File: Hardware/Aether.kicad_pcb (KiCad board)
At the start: 2 copper layers, 66.5 x 26 mm, 83 parts, among them J1 PRGM, J2 CONN-2, J3 CONN-2, J4 CONN-2, J5 CONN-2, J6 CONN-3, J7 CONN-3, Q1 IRLML6401, U1 ANTENOVA-UB, U2 ADF7012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

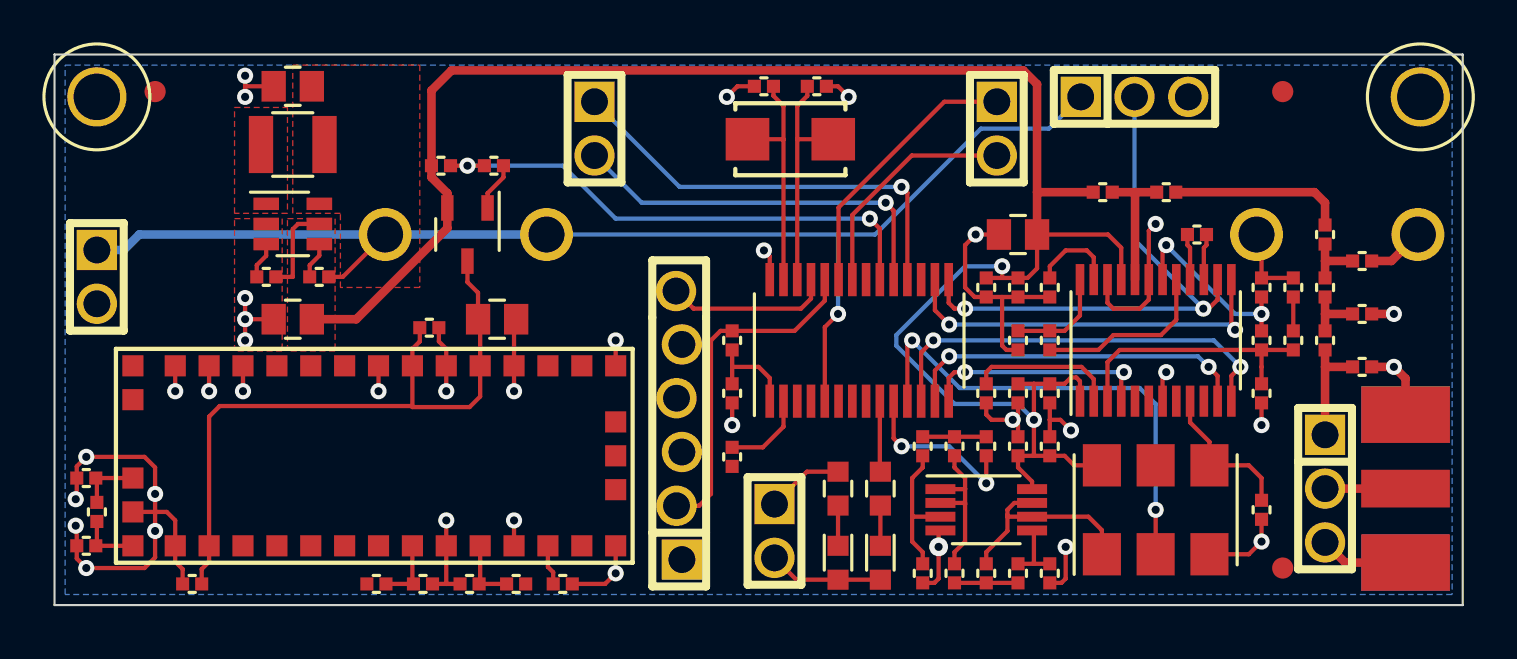
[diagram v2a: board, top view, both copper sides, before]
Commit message: Add RF ground pour
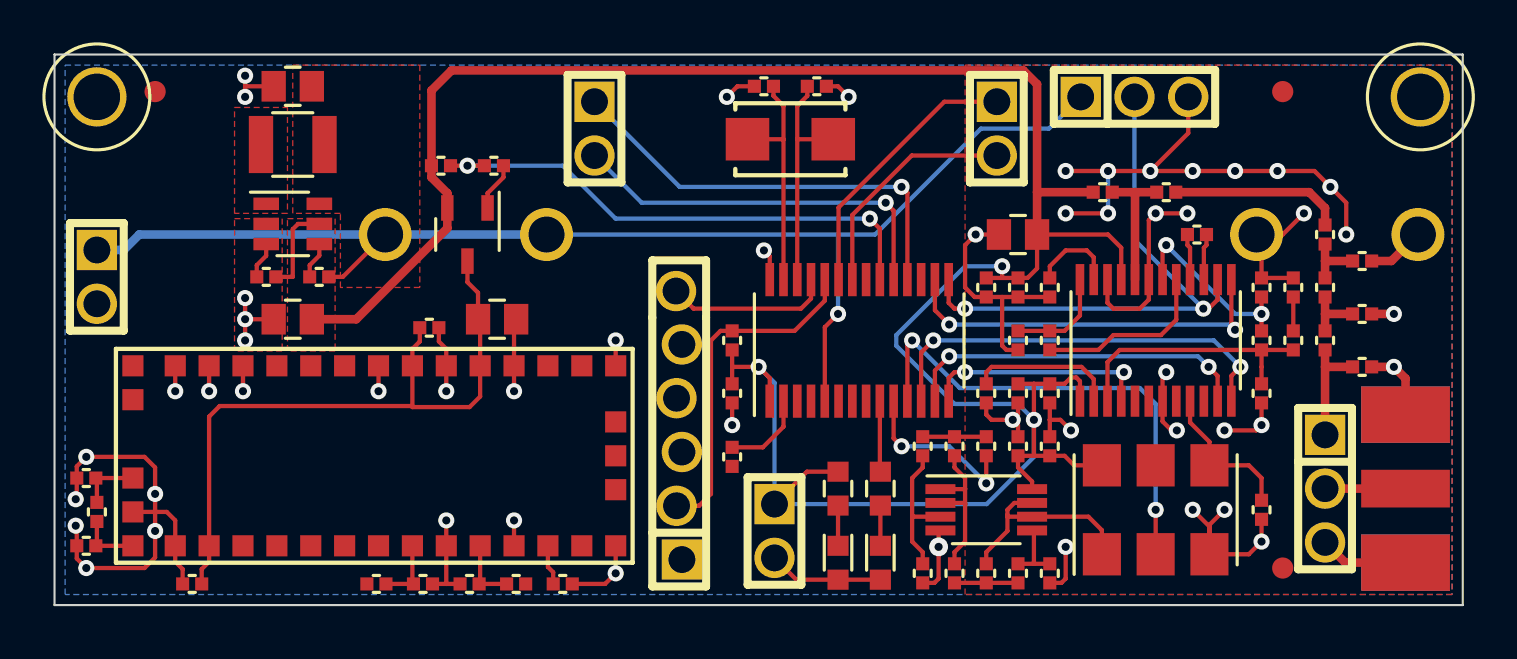
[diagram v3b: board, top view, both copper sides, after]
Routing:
- net GND: track 110.5 -> 147.3 mm, vias 36 -> 52
- net +3.3V: track 107.4 -> 129.1 mm, vias 2 -> 3
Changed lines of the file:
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@@
 (kicad_pcb (version 3) (host pcbnew "(2013-07-07 BZR 4022)-stable")
   (general
-    (links 0)
-    (no_connects 9)
+    (links 182)
+    (no_connects 7)
     (area 123.555134 93.0644 207.293981 122.9356)
     (thickness 1.6)
     (drawings 4)
-    (tracks 479)
+    (tracks 526)
     (zones 0)
     (modules 83)
@@
   (gr_line (start 195 121) (end 195 95) (angle 90) (layer Edge.Cuts) (width 0.1))
   (gr_line (start 128.5 121) (end 195 121) (angle 90) (layer Edge.Cuts) (width 0.1))
-  (segment (start 151.8 118.2) (end 151.8 119.2) (width 0.2032) (layer F.Cu) (net 1))
-  (segment (start 151.8 119.2) (end 152.05 119.45) (width 0.2032) (layer F.Cu) (net 1))
-  (segment (start 152.05 119.45) (end 152.05 120) (width 0.2032) (layer F.Cu) (net 1))
+  (segment (start 162.5 116.23) (end 172.52 116.23) (width 0.2032) (layer B.Cu) (net 1) (status 400000))
+  (segment (start 174.75 114) (end 174.75 112.25) (width 0.2032) (layer B.Cu) (net 1))
+  (segment (start 172.52 116.23) (end 174.75 114) (width 0.2032) (layer B.Cu) (net 1))
   (segment (start 168.25 108.25) (end 168.25 108.75) (width 0.2032) (layer B.Cu) (net 1))
-  (segment (start 174.75 112.25) (end 174 111.5) (width 0.2032) (layer B.Cu) (net 1))
   (segment (start 174 111.5) (end 171 111.5) (width 0.2032) (layer B.Cu) (net 1))
+  (segment (start 174 111.5) (end 174.75 112.25) (width 0.2032) (layer B.Cu) (net 1))
+  (segment (start 173.25 105.55) (end 173.25 105) (width 0.2032) (layer F.Cu) (net 1))
+  (via (at 173.25 105) (size 0.762) (layers F.Cu B.Cu) (net 1))
+  (segment (start 171.5 105) (end 173.25 105) (width 0.2032) (layer B.Cu) (net 1))
   (segment (start 171 111.5) (end 168.25 108.75) (width 0.2032) (layer B.Cu) (net 1))
-  (via (at 174.75 112.25) (size 0.762) (layers F.Cu B.Cu) (net 1))
   (segment (start 168.25 108.25) (end 171.5 105) (width 0.2032) (layer B.Cu) (net 1))
-  (segment (start 171.5 105) (end 173.25 105) (width 0.2032) (layer B.Cu) (net 1))
-  (via (at 173.25 105) (size 0.762) (layers F.Cu B.Cu) (net 1))
-  (segment (start 173.25 105) (end 173.25 105.55) (width 0.2032) (layer F.Cu) (net 1))
+  (via (at 174.75 112.25) (size 0.762) (layers F.Cu B.Cu) (net 1))
+  (segment (start 162.5 116.23) (end 162.5 110.5) (width 0.2032) (layer B.Cu) (net 1))
+  (via (at 161.75 109.75) (size 0.762) (layers F.Cu B.Cu) (net 1))
+  (segment (start 162.5 110.5) (end 161.75 109.75) (width 0.2032) (layer B.Cu) (net 1))
+  (segment (start 151.8 118.2) (end 151.8 119.2) (width 0.2032) (layer F.Cu) (net 1))
+  (segment (start 151.8 119.2) (end 152.05 119.45) (width 0.2032) (layer F.Cu) (net 1))
+  (segment (start 152.05 119.45) (end 152.05 120) (width 0.2032) (layer F.Cu) (net 1))
   (segment (start 160.5 109.75) (end 161.75 109.75) (width 0.2032) (layer F.Cu) (net 1))
   (segment (start 162.275 110.275) (end 162.275 111.37) (width 0.2032) (layer F.Cu) (net 1))
@@
   (segment (start 185.5 108.05) (end 185.5 107.25) (width 0.2032) (layer F.Cu) (net 31))
   (segment (start 185.5 107.25) (end 185.5 106.45) (width 0.2032) (layer F.Cu) (net 31))
+  (segment (start 178.25 100.5) (end 178.25 102.5) (width 0.2032) (layer B.Cu) (net 32))
+  (via (at 178.25 100.5) (size 0.762) (layers F.Cu B.Cu) (net 32))
+  (via (at 176.25 102.5) (size 0.762) (layers F.Cu B.Cu) (net 32))
+  (segment (start 178.25 102.5) (end 176.25 102.5) (width 0.2032) (layer F.Cu) (net 32))
+  (via (at 178.25 102.5) (size 0.762) (layers F.Cu B.Cu) (net 32))
+  (segment (start 176.25 100.5) (end 178.25 100.5) (width 0.2032) (layer F.Cu) (net 32))
+  (via (at 180.25 100.5) (size 0.762) (layers F.Cu B.Cu) (net 32))
+  (segment (start 178.25 100.5) (end 180.25 100.5) (width 0.2032) (layer F.Cu) (net 32))
+  (via (at 176.25 100.5) (size 0.762) (layers F.Cu B.Cu) (net 32))
+  (segment (start 183.04 118.6) (end 183.04 117.21) (width 0.2032) (layer F.Cu) (net 32) (status 400000))
+  (via (at 183.75 116.5) (size 0.762) (layers F.Cu B.Cu) (net 32))
+  (segment (start 183.04 117.21) (end 183.75 116.5) (width 0.2032) (layer F.Cu) (net 32))
+  (segment (start 183.04 118.6) (end 183.04 117.29) (width 0.2032) (layer F.Cu) (net 32) (status 400000))
+  (via (at 182.25 116.5) (size 0.762) (layers F.Cu B.Cu) (net 32))
+  (segment (start 183.04 117.29) (end 182.25 116.5) (width 0.2032) (layer F.Cu) (net 32))
+  (segment (start 180.825 111.37) (end 180.825 112.325) (width 0.2032) (layer F.Cu) (net 32) (status 400000))
+  (via (at 181.5 112.75) (size 0.762) (layers F.Cu B.Cu) (net 32))
+  (segment (start 181.25 112.75) (end 181.5 112.75) (width 0.2032) (layer F.Cu) (net 32))
+  (segment (start 180.825 112.325) (end 181.25 112.75) (width 0.2032) (layer F.Cu) (net 32))
+  (segment (start 185.5 112.5) (end 185.25 112.75) (width 0.2032) (layer F.Cu) (net 32))
+  (via (at 185.5 112.5) (size 0.762) (layers F.Cu B.Cu) (net 32))
+  (segment (start 185.5 111.45) (end 185.5 112.5) (width 0.2032) (layer F.Cu) (net 32))
+  (via (at 183.75 112.75) (size 0.762) (layers F.Cu B.Cu) (net 32))
+  (segment (start 185.25 112.75) (end 183.75 112.75) (width 0.2032) (layer F.Cu) (net 32))
+  (segment (start 185.265 103.5) (end 186.5 103.5) (width 0.2032) (layer F.Cu) (net 32) (status C00000))
+  (via (at 187.5 102.5) (size 0.762) (layers F.Cu B.Cu) (net 32))
+  (segment (start 186.5 103.5) (end 187.5 102.5) (width 0.2032) (layer F.Cu) (net 32) (status 400000))
+  (segment (start 182 102.5) (end 180.5 102.5) (width 0.2032) (layer F.Cu) (net 32))
+  (segment (start 180.175 102.825) (end 180.5 102.5) (width 0.2032) (layer F.Cu) (net 32))
+  (via (at 180.5 102.5) (size 0.762) (layers F.Cu B.Cu) (net 32))
+  (segment (start 180.175 102.825) (end 180.175 105.63) (width 0.2032) (layer F.Cu) (net 32) (status 800000))
+  (via (at 182 102.5) (size 0.762) (layers F.Cu B.Cu) (net 32))
+  (segment (start 188.75 101.25) (end 189.5 102) (width 0.2032) (layer F.Cu) (net 32))
+  (segment (start 188 100.5) (end 188.75 101.25) (width 0.2032) (layer F.Cu) (net 32))
+  (via (at 188.75 101.25) (size 0.762) (layers F.Cu B.Cu) (net 32))
+  (segment (start 186.25 100.5) (end 184.25 100.5) (width 0.2032) (layer F.Cu) (net 32))
+  (via (at 184.25 100.5) (size 0.762) (layers F.Cu B.Cu) (net 32))
+  (segment (start 182.25 100.5) (end 180.25 100.5) (width 0.2032) (layer F.Cu) (net 32))
+  (segment (start 182.04 98.71) (end 180.25 100.5) (width 0.2032) (layer F.Cu) (net 32))
+  (segment (start 182.04 97) (end 182.04 98.71) (width 0.2032) (layer F.Cu) (net 32) (status 400000))
+  (via (at 182.25 100.5) (size 0.762) (layers F.Cu B.Cu) (net 32))
+  (segment (start 184.25 100.5) (end 182.25 100.5) (width 0.2032) (layer F.Cu) (net 32))
+  (via (at 186.25 100.5) (size 0.762) (layers F.Cu B.Cu) (net 32))
+  (segment (start 186.25 100.5) (end 188 100.5) (width 0.2032) (layer F.Cu) (net 32))
+  (via (at 189.5 103.5) (size 0.762) (layers F.Cu B.Cu) (net 32))
+  (segment (start 189.5 102) (end 189.5 103.5) (width 0.2032) (layer F.Cu) (net 32))
   (segment (start 130 114) (end 132.75 114) (width 0.2032) (layer F.Cu) (net 32))
   (via (at 133.25 115.75) (size 0.762) (layers F.Cu B.Cu) (net 32))
@@
   (segment (start 190.7 104.75) (end 191.635 104.75) (width 0.4064) (layer F.Cu) (net 32))
   (segment (start 191.635 104.75) (end 192.885 103.5) (width 0.4064) (layer F.Cu) (net 32))
-  (segment (start 185.5 111.45) (end 185.5 112.5) (width 0.2032) (layer F.Cu) (net 32))
-  (via (at 185.5 112.5) (size 0.762) (layers F.Cu B.Cu) (net 32))
   (segment (start 185.5 116.95) (end 185.5 118) (width 0.2032) (layer F.Cu) (net 32))
   (segment (start 184.9 118.6) (end 185.5 118) (width 0.2032) (layer F.Cu) (net 32))
@@
   (segment (start 172.5 106.45) (end 173.25 106.45) (width 0.2032) (layer F.Cu) (net 32))
   (segment (start 173.25 106.45) (end 174 106.45) (width 0.2032) (layer F.Cu) (net 32))
-  (segment (start 180.175 105.63) (end 180.175 103.325) (width 0.2032) (layer F.Cu) (net 32))
-  (via (at 180.5 103) (size 0.762) (layers F.Cu B.Cu) (net 32))
-  (segment (start 180.175 103.325) (end 180.5 103) (width 0.2032) (layer F.Cu) (net 32))
   (segment (start 180.175 105.63) (end 180.175 106.575) (width 0.2032) (layer F.Cu) (net 32))
   (segment (start 178.225 106.725) (end 178.5 107) (width 0.2032) (layer F.Cu) (net 32))
@@
   (segment (start 188.5 103.95) (end 188.5 104.75) (width 0.4064) (layer F.Cu) (net 47))
   (segment (start 188.5 104.75) (end 188.5 105.55) (width 0.4064) (layer F.Cu) (net 47))
-  (segment (start 181.45 101.5) (end 188 101.5) (width 0.4064) (layer F.Cu) (net 48))
-  (segment (start 188 101.5) (end 188.5 102) (width 0.4064) (layer F.Cu) (net 48))
-  (segment (start 188.5 102) (end 188.5 103.05) (width 0.4064) (layer F.Cu) (net 48))
+  (segment (start 181.45 101.5) (end 187.75 101.5) (width 0.4064) (layer F.Cu) (net 48) (status 400000))
+  (segment (start 188.5 102.25) (end 188.5 103.05) (width 0.4064) (layer F.Cu) (net 48) (status 800000))
+  (segment (start 187.75 101.5) (end 188.5 102.25) (width 0.4064) (layer F.Cu) (net 48))
   (segment (start 187 108.05) (end 187 106.45) (width 0.2032) (layer F.Cu) (net 49))
   (segment (start 183.04 114.4) (end 184.9 114.4) (width 0.2032) (layer F.Cu) (net 50))
@@
       )
     )
+  )
+  (zone (net 32) (net_name GND) (layer F.Cu) (hatch edge 0.508)
+    (connect_pads (clearance 0.2032))
+    (min_thickness 0.2032)
+    (fill (arc_segments 16) (thermal_gap 0.2032) (thermal_bridge_width 0.3048))
+    (polygon
+      (pts
+        (xy 194.5 120.5) (xy 171.5 120.5) (xy 171.5 95.5) (xy 194.5 95.5)
+      )
+    )

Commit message: Finish layout
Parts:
- renumbered FIDUCIAL-1MM to FIDUCIAL-1MM-1, FIDUCIAL-1MM to FIDUCIAL-1MM-2, FIDUCIAL-1MM to FIDUCIAL-1MM-3, MECH-HOLE220 to MECH-HOLE220-1, MECH-HOLE220 to MECH-HOLE220-2
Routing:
- net /Core/GPS_Perf: track 0.00 -> 38.4 mm, vias 0 -> 2
- net /Core/RX: track 0.00 -> 28.7 mm, vias 0 -> 2
- net /GPS/RX: track 0.00 -> 22.8 mm, vias 0 -> 2
- net +3.3V: track 129.1 -> 140.6 mm
- net +5V: track 0.00 -> 4.14 mm, vias 0 -> 1
- net N-0000030: track 31.8 -> 30.9 mm
